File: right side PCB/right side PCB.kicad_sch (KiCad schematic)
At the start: 8 parts

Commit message: right conn mother
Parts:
- removed U?: power_btr, mother_conn_side:conn_side, symbol conn_mother_side:power_btr
- gave numbers to parts that had none: 7
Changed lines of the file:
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@@
   (symbol (lib_id "conn_mother_side:power_btr") (at 138.43 116.84 270) (unit 1)
     (in_bom yes) (on_board yes) (fields_autoplaced)
-    (property "Reference" "U?" (id 0) (at 139.7 120.6499 90)
+    (property "Reference" "U6" (id 0) (at 139.7 120.6499 90)
       (effects (font (size 1.27 1.27)) (justify left))
     )
@@
   (symbol (lib_id "conn_mother_side:power_btr") (at 95.25 116.84 270) (unit 1)
     (in_bom yes) (on_board yes) (fields_autoplaced)
-    (property "Reference" "U?" (id 0) (at 96.52 120.6499 90)
+    (property "Reference" "U3" (id 0) (at 96.52 120.6499 90)
       (effects (font (size 1.27 1.27)) (justify left))
     )
@@
   (symbol (lib_id "conn_mother_side:battery") (at 142.24 90.17 180) (unit 1)
     (in_bom yes) (on_board yes) (fields_autoplaced)
-    (property "Reference" "U?" (id 0) (at 137.795 82.55 0))
+    (property "Reference" "U7" (id 0) (at 137.795 82.55 0))
     (property "Value" "battery" (id 1) (at 137.795 85.09 0))
     (property "Footprint" "mother_conn_side:btttr" (id 2) (at 142.24 90.17 0)
@@
   (symbol (lib_id "conn_mother_side:power_btr") (at 110.49 116.84 270) (unit 1)
     (in_bom yes) (on_board yes) (fields_autoplaced)
-    (property "Reference" "U?" (id 0) (at 111.76 120.6499 90)
+    (property "Reference" "U4" (id 0) (at 111.76 120.6499 90)
       (effects (font (size 1.27 1.27)) (justify left))
     )
@@
   (symbol (lib_id "conn_mother_side:power_btr") (at 124.46 116.84 270) (unit 1)
     (in_bom yes) (on_board yes) (fields_autoplaced)
-    (property "Reference" "U?" (id 0) (at 125.73 120.6499 90)
+    (property "Reference" "U5" (id 0) (at 125.73 120.6499 90)
       (effects (font (size 1.27 1.27)) (justify left))
     )
@@
   (symbol (lib_id "conn_mother_side:battery") (at 93.98 88.9 0) (unit 1)
     (in_bom yes) (on_board yes) (fields_autoplaced)
-    (property "Reference" "U?" (id 0) (at 101.6 87.6299 0)
+    (property "Reference" "U2" (id 0) (at 101.6 87.6299 0)
       (effects (font (size 1.27 1.27)) (justify left))
     )
@@
   (symbol (lib_id "conn_mother_side:power_btr") (at 81.28 116.84 270) (unit 1)
     (in_bom yes) (on_board yes) (fields_autoplaced)
-    (property "Reference" "U?" (id 0) (at 82.55 120.6499 90)
+    (property "Reference" "U1" (id 0) (at 82.55 120.6499 90)
       (effects (font (size 1.27 1.27)) (justify left))
     )
@@
     (pin "1")
   )
-  (symbol (lib_id "conn_mother_side:power_btr") (at 151.13 116.84 270) (unit 1)
-    (in_bom yes) (on_board yes) (fields_autoplaced)
-    (property "Reference" "U?" (id 0) (at 152.4 120.6499 90)
-      (effects (font (size 1.27 1.27)) (justify left))
-    )
-    (property "Value" "power_btr" (id 1) (at 152.4 123.1899 90)
-      (effects (font (size 1.27 1.27)) (justify left))
-    )
-    (property "Footprint" "mother_conn_side:conn_side" (id 2) (at 151.13 116.84 0)
-      (effects (font (size 1.27 1.27)) hide)
-    )
-    (property "Datasheet" "" (id 3) (at 151.13 116.84 0)
-      (effects (font (size 1.27 1.27)) hide)
-    )
-    (pin "1")
-  )
   (sheet_instances
     (path "/" (page "1"))
   )
   (symbol_instances
-    (path "/0aac861c-e6fd-4e49-904d-30464dc91a02"
-      (reference "U?") (unit 1) (value "power_btr") (footprint "mother_conn_side:conn_side")
+    (path "/e2ffa247-f3cf-4966-b880-52558324ad1f"
+      (reference "U1") (unit 1) (value "power_btr") (footprint "mother_conn_side:conn_side")
+    )
+    (path "/e2d83c5e-523a-4f60-994e-3139c5df75a4"
+      (reference "U2") (unit 1) (value "battery") (footprint "mother_conn_side:btttr")
     )
     (path "/1f425f94-1fb7-44c4-a040-7b97662dd0ac"
-      (reference "U?") (unit 1) (value "power_btr") (footprint "mother_conn_side:conn_side")
+      (reference "U3") (unit 1) (value "power_btr") (footprint "mother_conn_side:conn_side")
+    )
+    (path "/671f8980-5c19-4691-b9f7-d847d34ad046"
+      (reference "U4") (unit 1) (value "power_btr") (footprint "mother_conn_side:conn_side")
+    )
+    (path "/d56c24cd-18a2-4ffa-867b-44f80c7cdc8b"
+      (reference "U5") (unit 1) (value "power_btr") (footprint "mother_conn_side:conn_side")
+    )
+    (path "/0aac861c-e6fd-4e49-904d-30464dc91a02"
+      (reference "U6") (unit 1) (value "power_btr") (footprint "mother_conn_side:conn_side")
     )
     (path "/339af272-b753-45be-a8f1-5e3de643d818"
-      (reference "U?") (unit 1) (value "battery") (footprint "mother_conn_side:btttr")
-    )
-    (path "/671f8980-5c19-4691-b9f7-d847d34ad046"
-      (reference "U?") (unit 1) (value "power_btr") (footprint "mother_conn_side:conn_side")
-    )
-    (path "/d56c24cd-18a2-4ffa-867b-44f80c7cdc8b"
-      (reference "U?") (unit 1) (value "power_btr") (footprint "mother_conn_side:conn_side")
-    )
-    (path "/e2d83c5e-523a-4f60-994e-3139c5df75a4"
-      (reference "U?") (unit 1) (value "battery") (footprint "mother_conn_side:btttr")
-    )
-    (path "/e2ffa247-f3cf-4966-b880-52558324ad1f"
-      (reference "U?") (unit 1) (value "power_btr") (footprint "mother_conn_side:conn_side")
-    )
-    (path "/efd7a1e0-5bed-4583-a94e-5ccec9e4eb74"
-      (reference "U?") (unit 1) (value "power_btr") (footprint "mother_conn_side:conn_side")
+      (reference "U7") (unit 1) (value "battery") (footprint "mother_conn_side:btttr")
     )
   )

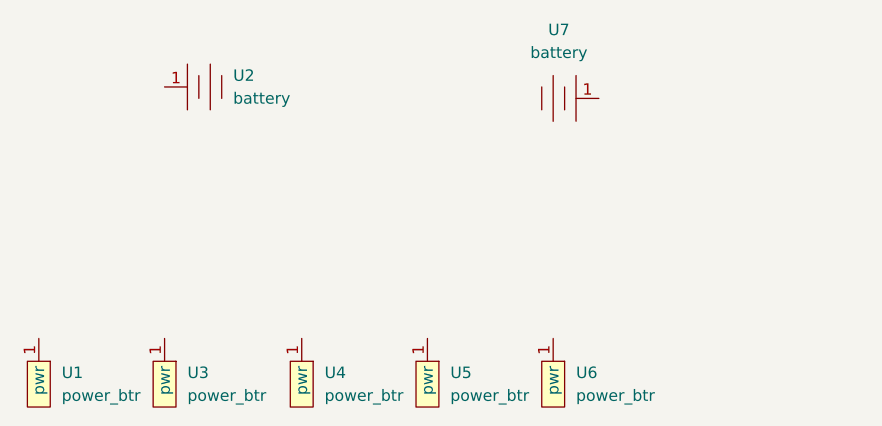
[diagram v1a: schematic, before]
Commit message: add led conn pcb
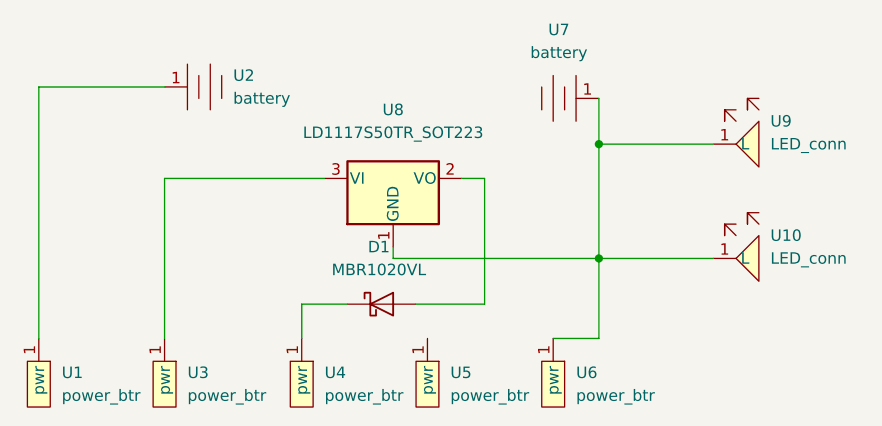
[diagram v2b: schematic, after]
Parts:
- added D1: MBR1020VL, Diode_SMD:D_SOD-123F, symbol Diode:MBR1020VL
- added U10, U9: LED_conn, mother_conn_side:led_conn, symbol conn_mother_side:LED_conn
- added U8: LD1117S50TR_SOT223, Package_TO_SOT_SMD:SOT-223-3_TabPin2, symbol Regulator_Linear:LD1117S50TR_SOT223
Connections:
- net at U6.1 (pwr): now also U7.1, U10.1 (L), U8.1 (GND), U9.1 (L)
- net at U3.1 (pwr): now also U8.3 (VI)
- net at U4.1 (pwr): now also D1.1 (K)
- net at U2.1: now also U1.1 (pwr)
- new net: D1.2 (A), U8.2 (VO)
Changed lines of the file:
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@@
 (kicad_sch (version 20211123) (generator eeschema)
   (paper "A4")
+  (junction (at 142.24 95.25) (diameter 0) (color 0 0 0 0)
+  )
+  (junction (at 142.24 107.95) (diameter 0) (color 0 0 0 0)
+  )
+  (wire (pts (xy 93.98 116.84) (xy 93.98 99.06))
+    (stroke (width 0) (type default) (color 0 0 0 0))
+  )
+  (wire (pts (xy 129.54 99.06) (xy 129.54 113.03))
+    (stroke (width 0) (type default) (color 0 0 0 0))
+  )
+  (wire (pts (xy 142.24 107.95) (xy 119.38 107.95))
+    (stroke (width 0) (type default) (color 0 0 0 0))
+  )
+  (wire (pts (xy 142.24 107.95) (xy 142.24 116.84))
+    (stroke (width 0) (type default) (color 0 0 0 0))
+  )
+  (wire (pts (xy 127 99.06) (xy 129.54 99.06))
+    (stroke (width 0) (type default) (color 0 0 0 0))
+  )
+  (wire (pts (xy 142.24 107.95) (xy 154.94 107.95))
+    (stroke (width 0) (type default) (color 0 0 0 0))
+  )
+  (wire (pts (xy 142.24 90.17) (xy 142.24 95.25))
+    (stroke (width 0) (type default) (color 0 0 0 0))
+  )
+  (wire (pts (xy 137.16 116.84) (xy 142.24 116.84))
+    (stroke (width 0) (type default) (color 0 0 0 0))
+  )
+  (wire (pts (xy 80.01 88.9) (xy 93.98 88.9))
+    (stroke (width 0) (type default) (color 0 0 0 0))
+  )
+  (wire (pts (xy 142.24 95.25) (xy 154.94 95.25))
+    (stroke (width 0) (type default) (color 0 0 0 0))
+  )
+  (wire (pts (xy 93.98 99.06) (xy 111.76 99.06))
+    (stroke (width 0) (type default) (color 0 0 0 0))
+  )
+  (wire (pts (xy 121.92 113.03) (xy 129.54 113.03))
+    (stroke (width 0) (type default) (color 0 0 0 0))
+  )
+  (wire (pts (xy 142.24 95.25) (xy 142.24 107.95))
+    (stroke (width 0) (type default) (color 0 0 0 0))
+  )
+  (wire (pts (xy 109.22 113.03) (xy 114.3 113.03))
+    (stroke (width 0) (type default) (color 0 0 0 0))
+  )
+  (wire (pts (xy 80.01 116.84) (xy 80.01 88.9))
+    (stroke (width 0) (type default) (color 0 0 0 0))
+  )
+  (wire (pts (xy 119.38 107.95) (xy 119.38 106.68))
+    (stroke (width 0) (type default) (color 0 0 0 0))
+  )
+  (wire (pts (xy 109.22 113.03) (xy 109.22 116.84))
+    (stroke (width 0) (type default) (color 0 0 0 0))
+  )
   (symbol (lib_id "conn_mother_side:power_btr") (at 138.43 116.84 270) (unit 1)
     (in_bom yes) (on_board yes) (fields_autoplaced)
@@
     (pin "1")
   )
+  (symbol (lib_id "Diode:MBR1020VL") (at 118.11 113.03 0) (unit 1)
+    (in_bom yes) (on_board yes) (fields_autoplaced)
+    (property "Reference" "D1" (id 0) (at 117.7925 106.68 0))
+    (property "Value" "MBR1020VL" (id 1) (at 117.7925 109.22 0))
+    (property "Footprint" "Diode_SMD:D_SOD-123F" (id 2) (at 118.11 117.475 0)
+      (effects (font (size 1.27 1.27)) hide)
+    )
+    (property "Datasheet" "https://www.onsemi.com/pub/Collateral/MBR1020VL-D.PDF" (id 3) (at 118.11 113.03 0)
+      (effects (font (size 1.27 1.27)) hide)
+    )
+    (pin "1")
+    (pin "2")
+  )
   (symbol (lib_id "conn_mother_side:power_btr") (at 110.49 116.84 270) (unit 1)
     (in_bom yes) (on_board yes) (fields_autoplaced)
@@
     (pin "1")
   )
+  (symbol (lib_id "conn_mother_side:LED_conn") (at 154.94 95.25 0) (unit 1)
+    (in_bom yes) (on_board yes) (fields_autoplaced)
+    (property "Reference" "U9" (id 0) (at 161.29 92.7099 0)
+      (effects (font (size 1.27 1.27)) (justify left))
+    )
+    (property "Value" "LED_conn" (id 1) (at 161.29 95.2499 0)
+      (effects (font (size 1.27 1.27)) (justify left))
+    )
+    (property "Footprint" "mother_conn_side:led_conn" (id 2) (at 154.94 95.25 0)
+      (effects (font (size 1.27 1.27)) hide)
+    )
+    (property "Datasheet" "" (id 3) (at 154.94 95.25 0)
+      (effects (font (size 1.27 1.27)) hide)
+    )
+    (pin "1")
+  )
+  (symbol (lib_id "Regulator_Linear:LD1117S50TR_SOT223") (at 119.38 99.06 0) (unit 1)
+    (in_bom yes) (on_board yes) (fields_autoplaced)
+    (property "Reference" "U8" (id 0) (at 119.38 91.44 0))
+    (property "Value" "LD1117S50TR_SOT223" (id 1) (at 119.38 93.98 0))
+    (property "Footprint" "Package_TO_SOT_SMD:SOT-223-3_TabPin2" (id 2) (at 119.38 93.98 0)
+      (effects (font (size 1.27 1.27)) hide)
+    )
+    (property "Datasheet" "http://www.st.com/st-web-ui/static/active/en/resource/technical/document/datasheet/CD00000544.pdf" (id 3) (at 121.92 105.41 0)
+      (effects (font (size 1.27 1.27)) hide)
+    )
+    (pin "1")
+    (pin "2")
+    (pin "3")
+  )
   (symbol (lib_id "conn_mother_side:power_btr") (at 124.46 116.84 270) (unit 1)
     (in_bom yes) (on_board yes) (fields_autoplaced)
@@
     )
     (property "Datasheet" "" (id 3) (at 124.46 116.84 0)
+      (effects (font (size 1.27 1.27)) hide)
+    )
+    (pin "1")
+  )
+  (symbol (lib_id "conn_mother_side:LED_conn") (at 154.94 107.95 0) (unit 1)
+    (in_bom yes) (on_board yes) (fields_autoplaced)
+    (property "Reference" "U10" (id 0) (at 161.29 105.4099 0)
+      (effects (font (size 1.27 1.27)) (justify left))
+    )
+    (property "Value" "LED_conn" (id 1) (at 161.29 107.9499 0)
+      (effects (font (size 1.27 1.27)) (justify left))
+    )
+    (property "Footprint" "mother_conn_side:led_conn" (id 2) (at 154.94 107.95 0)
+      (effects (font (size 1.27 1.27)) hide)
+    )
+    (property "Datasheet" "" (id 3) (at 154.94 107.95 0)
       (effects (font (size 1.27 1.27)) hide)
     )
@@
   )
   (symbol_instances
+    (path "/37081654-8f99-4a40-95a5-cb89ab90304e"
+      (reference "D1") (unit 1) (value "MBR1020VL") (footprint "Diode_SMD:D_SOD-123F")
+    )
     (path "/e2ffa247-f3cf-4966-b880-52558324ad1f"
       (reference "U1") (unit 1) (value "power_btr") (footprint "mother_conn_side:conn_side")
@@
       (reference "U7") (unit 1) (value "battery") (footprint "mother_conn_side:btttr")
     )
-  )
+    (path "/d01102e9-b170-4eb1-a0a4-9a31feb850b7"
+      (reference "U8") (unit 1) (value "LD1117S50TR_SOT223") (footprint "Package_TO_SOT_SMD:SOT-223-3_TabPin2")
+    )
+    (path "/6df433d7-73cd-4877-8d2e-047853b9077c"
+      (reference "U9") (unit 1) (value "LED_conn") (footprint "mother_conn_side:led_conn")
+    )
+    (path "/e0fafb5a-7612-49f2-857e-07a48cf36c67"
+      (reference "U10") (unit 1) (value "LED_conn") (footprint "mother_conn_side:led_conn")
+    )
+  )
